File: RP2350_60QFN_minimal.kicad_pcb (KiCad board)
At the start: 2 copper layers, 52 x 51 mm, 43 parts, among them J1 USB_B_Micro, J2 Conn_02x18_Odd_Even, J3 Conn_02x18_Odd_Even, J4 SM03B-SRSS-TB, SW1 SW_Push, SW2 SW_Push, U1 RP2350_60QFN, U2 NCP1117-3.3_SOT223, U3 W25Q128JVS, Y1 ABM8-272-T3

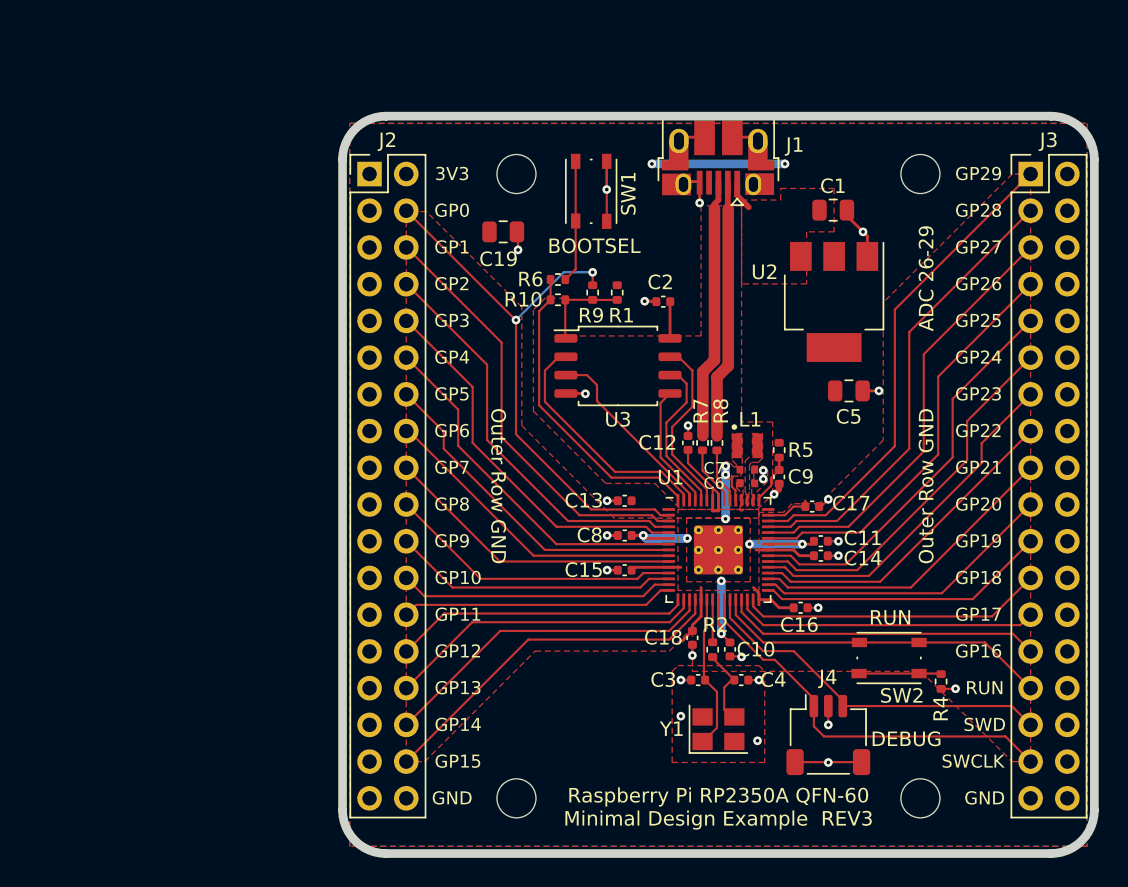
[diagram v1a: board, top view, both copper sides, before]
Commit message: try to place components
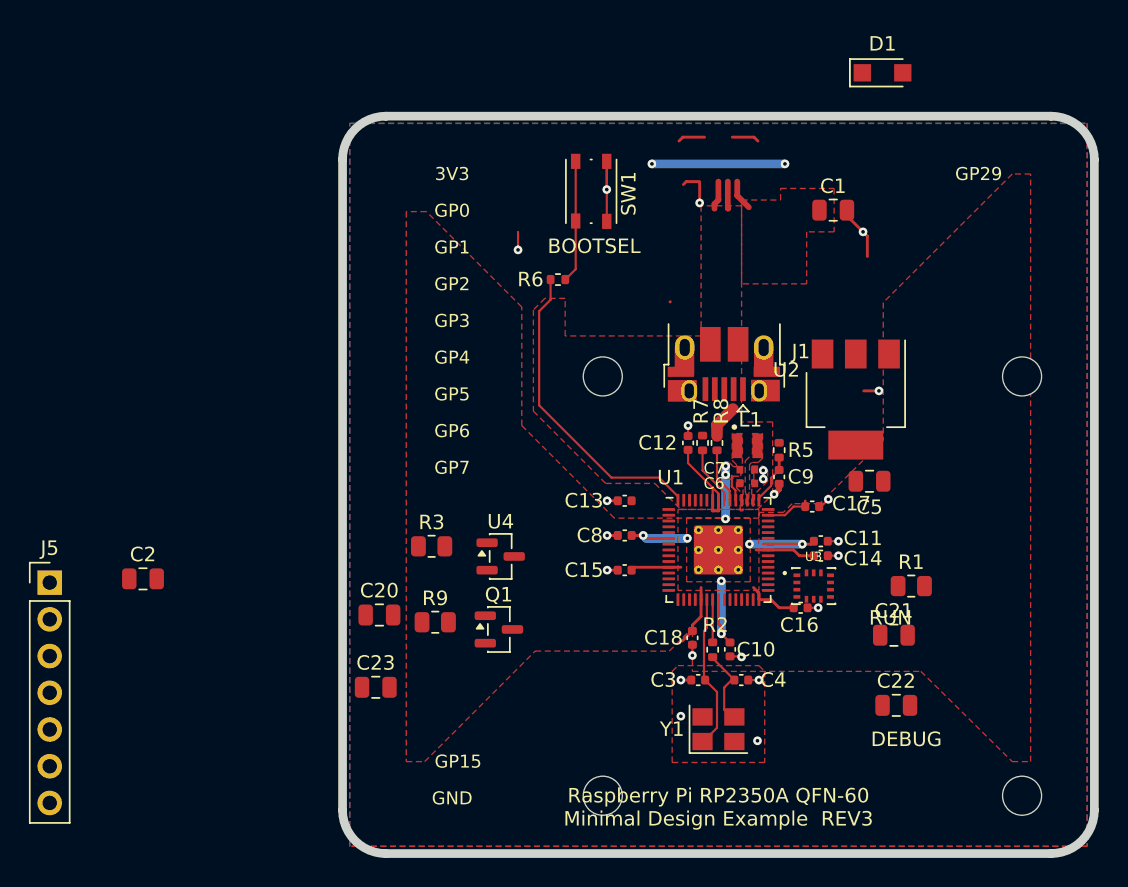
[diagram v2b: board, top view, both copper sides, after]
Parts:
- removed C19: 10u, Capacitor_SMD:C_0805_2012Metric
- removed J2, J3: Conn_02x18_Odd_Even, Connector_PinHeader_2.54mm:PinHeader_2x18_P2.54mm_Vertical
- removed J4: SM03B-SRSS-TB, Connector_JST:JST_SH_SM03B-SRSS-TB_1x03-1MP_P1.00mm_Horizontal
- removed R10: 0, Resistor_SMD:R_0402_1005Metric
- removed R4: 1k, Resistor_SMD:R_0402_1005Metric
- removed SW2: SW_Push, Button_Switch_SMD:SW_Push_1P1T_NO_Vertical_Wuerth_434133025816
- added C20: 1u, Capacitor_SMD:C_0805_2012Metric, F.Cu at (76.5, 104.5)
- added C21: 100n, Capacitor_SMD:C_0805_2012Metric, F.Cu at (112.1, 105.9)
- added C22: 100n, Capacitor_SMD:C_0805_2012Metric, F.Cu at (112.3, 110.8)
- added C23: 1u, Capacitor_SMD:C_0805_2012Metric, F.Cu at (76.3, 109.5)
- added D1: PMEG3010ER, Diode_SMD:Nexperia_CFP3_SOD-123W, F.Cu at (111.3, 67.0)
- added J5: Conn_01x07, Connector_PinHeader_2.54mm:PinHeader_1x07_P2.54mm_Vertical, F.Cu at (53.8, 102.3)
- added Q1: BSS138, Package_TO_SOT_SMD:SOT-23, F.Cu at (84.8, 105.5)
- added R3: 10k, Resistor_SMD:R_0805_2012Metric, F.Cu at (80.2, 99.8)
- added U4: MCP1700T-1802E/TT, Package_TO_SOT_SMD:SOT-23, F.Cu at (84.9, 100.5)
- C2: value 100n -> 10u; footprint Capacitor_SMD:C_0402_1005Metric -> Capacitor_SMD:C_0805_2012Metric
- R1: value DNF -> 100k; footprint Resistor_SMD:R_0402_1005Metric -> Resistor_SMD:R_0805_2012Metric
- R9: value DNF -> 10k; footprint Resistor_SMD:R_0402_1005Metric -> Resistor_SMD:R_0805_2012Metric
- U3: value W25Q128JVS -> BMI270; footprint Package_SO:SOIC-8_5.23x5.23mm_P1.27mm -> BMI270:XDCR_BMI270
- moved C2 40.8 mm to (60.2, 102.0), turned to 0 degrees
- moved H4 35.0 mm to (121.0, 117.0)
- moved R1 28.7 mm to (113.3, 102.5), turned to 0 degrees
- moved R9 25.3 mm to (80.4, 105.0), turned to 0 degrees
- moved H3 22.0 mm to (92.0, 117.0)
- moved U3 20.4 mm to (106.6, 102.5)
- moved H2 15.7 mm to (121.0, 88.0)
- moved H1 15.2 mm to (92.0, 88.0)
- moved J1 14.3 mm to (100.4, 87.1)
- moved U2 6.91 mm to (109.5, 89.6)
- moved C5 6.41 mm to (110.5, 95.2)
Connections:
- C1 pad 1: VBUS -> Net-(D1-A)
- C2 pad 1: +3V3 -> +5V
- J1 pad 1: VBUS -> Net-(D1-A)
- R1 pad 2: /FLASH_SS -> /IMU_CS
- R9 pad 1: /GPIO0 -> +3V3
- R9 pad 2: /FLASH_SS -> /XTR_3V3
- U1 pad 10: /GPIO7 -> unconnected-(U1-GPIO7-Pad10)
- U1 pad 12: /GPIO8 -> unconnected-(U1-GPIO8-Pad12)
- U1 pad 13: /GPIO9 -> unconnected-(U1-GPIO9-Pad13)
- U1 pad 14: /GPIO10 -> unconnected-(U1-GPIO10-Pad14)
- U1 pad 15: /GPIO11 -> unconnected-(U1-GPIO11-Pad15)
- U1 pad 16: /GPIO12 -> unconnected-(U1-GPIO12-Pad16)
- U1 pad 17: /GPIO13 -> /XTR_3V3
- U1 pad 19: /GPIO15 -> /IMU_INT1
- U1 pad 2: /GPIO0 -> /UART_TX
- U1 pad 26: /RUN -> unconnected-(U1-RUN-Pad26)
- U1 pad 27: /GPIO16 -> /IMU_MISO
- U1 pad 28: /GPIO17 -> /IMU_CS
- U1 pad 29: /GPIO18 -> /IMU_SCK
- U1 pad 3: /GPIO1 -> /UART_RX
- U1 pad 31: /GPIO19 -> /IMU_MOSI
- U1 pad 32: /GPIO20 -> unconnected-(U1-GPIO20-Pad32)
- U1 pad 33: /GPIO21 -> unconnected-(U1-GPIO21-Pad33)
- U1 pad 34: /GPIO22 -> unconnected-(U1-GPIO22-Pad34)
- U1 pad 35: /GPIO23 -> unconnected-(U1-GPIO23-Pad35)
- U1 pad 36: /GPIO24 -> unconnected-(U1-GPIO24-Pad36)
- U1 pad 37: /GPIO25 -> unconnected-(U1-GPIO25-Pad37)
- U1 pad 4: /GPIO2 -> unconnected-(U1-GPIO2-Pad4)
- U1 pad 40: /GPIO26_ADC0 -> unconnected-(U1-GPIO26_ADC0-Pad40)
- U1 pad 41: /GPIO27_ADC1 -> unconnected-(U1-GPIO27_ADC1-Pad41)
- U1 pad 42: /GPIO28_ADC2 -> unconnected-(U1-GPIO28_ADC2-Pad42)
- U1 pad 43: /GPIO29_ADC3 -> unconnected-(U1-GPIO29_ADC3-Pad43)
- U1 pad 5: /GPIO3 -> unconnected-(U1-GPIO3-Pad5)
- U1 pad 55: /QSPI_SD3 -> unconnected-(U1-QSPI_SD3-Pad55)
- U1 pad 56: /QSPI_SCLK -> unconnected-(U1-QSPI_SCLK-Pad56)
- U1 pad 57: /QSPI_SD0 -> unconnected-(U1-QSPI_SD0-Pad57)
- U1 pad 58: /QSPI_SD2 -> unconnected-(U1-QSPI_SD2-Pad58)
- U1 pad 59: /QSPI_SD1 -> unconnected-(U1-QSPI_SD1-Pad59)
- U1 pad 7: /GPIO4 -> unconnected-(U1-GPIO4-Pad7)
- U1 pad 8: /GPIO5 -> unconnected-(U1-GPIO5-Pad8)
- U1 pad 9: /GPIO6 -> unconnected-(U1-GPIO6-Pad9)
- U2 pad 3: VBUS -> +5V
- U3 pad 1: /FLASH_SS -> /IMU_MISO
- U3 pad 2: /QSPI_SD1 -> unconnected-(U3-ASDX-Pad2)
- U3 pad 3: /QSPI_SD2 -> unconnected-(U3-ASCX-Pad3)
- U3 pad 4: GND -> /IMU_INT1
- U3 pad 5: /QSPI_SD0 -> +3V3
- U3 pad 6: /QSPI_SCLK -> GND
- U3 pad 7: /QSPI_SD3 -> GND
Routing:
- net /GPIO0: track 39.0 -> 0.00 mm, vias 2 -> 0
- net /GPIO29_ADC3: track 33.6 -> 0.00 mm
- net /GPIO28_ADC2: track 31.9 -> 0.00 mm
- net /GPIO27_ADC1: track 30.3 -> 0.00 mm
- net /GPIO1: track 29.8 -> 0.00 mm
- net /GPIO26_ADC0: track 28.6 -> 0.00 mm
- net /GPIO2: track 28.2 -> 0.00 mm
- net /SWCLK: track 27.8 -> 0.00 mm
- net /GPIO25: track 27.7 -> 0.00 mm
- net /GPIO3: track 26.5 -> 0.00 mm
- net /GPIO24: track 26.1 -> 0.00 mm
- net /SWD: track 25.4 -> 0.00 mm
- net /GPIO15: track 25.2 -> 0.00 mm
- net /GPIO4: track 25.0 -> 0.00 mm
- net /GPIO23: track 24.4 -> 0.00 mm
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- added copper zone on F.Cu, net Net-(D1-A)
- removed copper zone on F.Cu, net VBUS
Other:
- board text removed: "ADC 26-29"
- board text removed: "GP10"
- board text removed: "GP11"
- board text removed: "GP12"
- board text removed: "GP13"
- board text removed: "GP14"
- board text removed: "GP16"
- board text removed: "GP17"
- board text removed: "GP18"
- board text removed: "GP19"
- board text removed: "GP20"
- board text removed: "GP21"
- board text removed: "GP22"
- board text removed: "GP23"
- board text removed: "GP24"
- board text removed: "GP25"
- board text removed: "GP26"
- board text removed: "GP27"
- board text removed: "GP28"
- board text removed: "GP8"
- board text removed: "GP9"
- board text removed: "Outer Row GND"
- board text removed: "SWCLK"
- board text removed: "SWD"

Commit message: working
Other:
- board text removed: "3V3"
- board text removed: "GP0"
- board text removed: "GP1"
- board text removed: "GP2"
- board text removed: "GP3"
- board text removed: "GP4"
- board text removed: "GP5"
- board text removed: "GP6"
- board text removed: "GP7"
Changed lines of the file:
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@@
 		(layer "Edge.Cuts")
-	)
-	(gr_text "GP1"
-		(at 81.585 79.08 0)
-		(layer "F.SilkS")
-		(effects
-			(font
-				(size 0.9 0.9)
-				(thickness 0.1)
-			)
-		)
-	)
-	(gr_text "GP2"
-		(at 81.585 81.62 0)
-		(layer "F.SilkS")
-		(effects
-			(font
-				(size 0.9 0.9)
-				(thickness 0.1)
-			)
-		)
-	)
-	(gr_text "GP3"
-		(at 81.585 84.16 0)
-		(layer "F.SilkS")
-		(effects
-			(font
-				(size 0.9 0.9)
-				(thickness 0.1)
-			)
-		)
-	)
-	(gr_text "GP4"
-		(at 81.585 86.7 0)
-		(layer "F.SilkS")
-		(effects
-			(font
-				(size 0.9 0.9)
-				(thickness 0.1)
-			)
-		)
-	)
-	(gr_text "GP5"
-		(at 81.585 89.24 0)
-		(layer "F.SilkS")
-		(effects
-			(font
-				(size 0.9 0.9)
-				(thickness 0.1)
-			)
-		)
-	)
-	(gr_text "GP6"
-		(at 81.585 91.78 0)
-		(layer "F.SilkS")
-		(effects
-			(font
-				(size 0.9 0.9)
-				(thickness 0.1)
-			)
-		)
-	)
-	(gr_text "GP7"
-		(at 81.585 94.32 0)
-		(layer "F.SilkS")
-		(effects
-			(font
-				(size 0.9 0.9)
-				(thickness 0.1)
-			)
-		)
 	)
 	(gr_text "GP15"
@@
 		)
 	)
-	(gr_text "3V3"
-		(at 81.585 74 0)
-		(layer "F.SilkS")
-		(effects
-			(font
-				(size 0.9 0.9)
-				(thickness 0.1)
-			)
-		)
-	)
 	(gr_text "DEBUG"
 		(at 113 113.1 0)
@@
 			)
 		)
-	)
-	(gr_text "GP0"
-		(at 81.585 76.54 0)
-		(layer "F.SilkS")
-		(effects
-			(font
-				(size 0.9 0.9)
-				(thickness 0.1)
-			)
-		)
